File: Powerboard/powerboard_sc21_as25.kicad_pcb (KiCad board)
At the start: 4 copper layers, 86.3 x 55.6 mm, 149 parts, among them IC1 BQ24618RGET-iclr, IC2 CP2102, J1 Thermistor Connection 103AT N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, J10 Conn_01x04_Male, J2 Conn_01x02_Male, J3 Conn_01x02_Male, J4 Conn_01x08_Male, J5 Conn_01x04_Male, J6 Conn_01x02_Male, J7 IsolationSwitch, J8 USB_C_Receptacle_USB2.0, J9 Conn_Coaxial, Q1 RSJ250P10TL, Q10 MCH6351, Q2 RSJ250P10TL, Q3 RSJ250P10TL, Q4 RS1G120MN, Q5 RS1G120MN, Q6 MMDT2222A, Q7 RSJ250P10TL, Q8 RSJ250P10TL, Q9 MCH6351, U1 LTC4412xS6, U11 LTC4411, U2 SN65HVD230, U3 ESP32-PICO-D4, U4 SC4216H, U6 LM2679T-3.3-iclr, U7 LM2679T-3.3-iclr, U8 LTC4412xS6, U9 LTC4412xS6

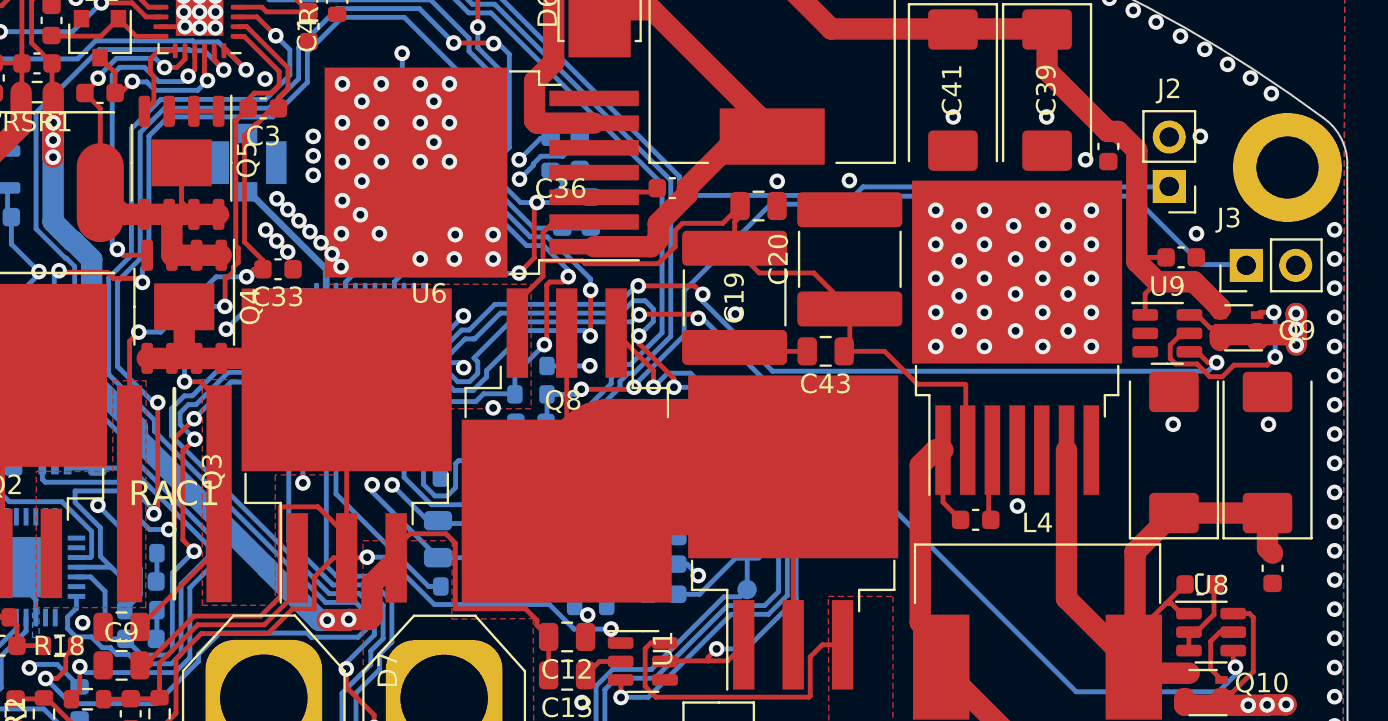
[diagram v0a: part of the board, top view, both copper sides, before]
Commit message: Removed CAN resistors
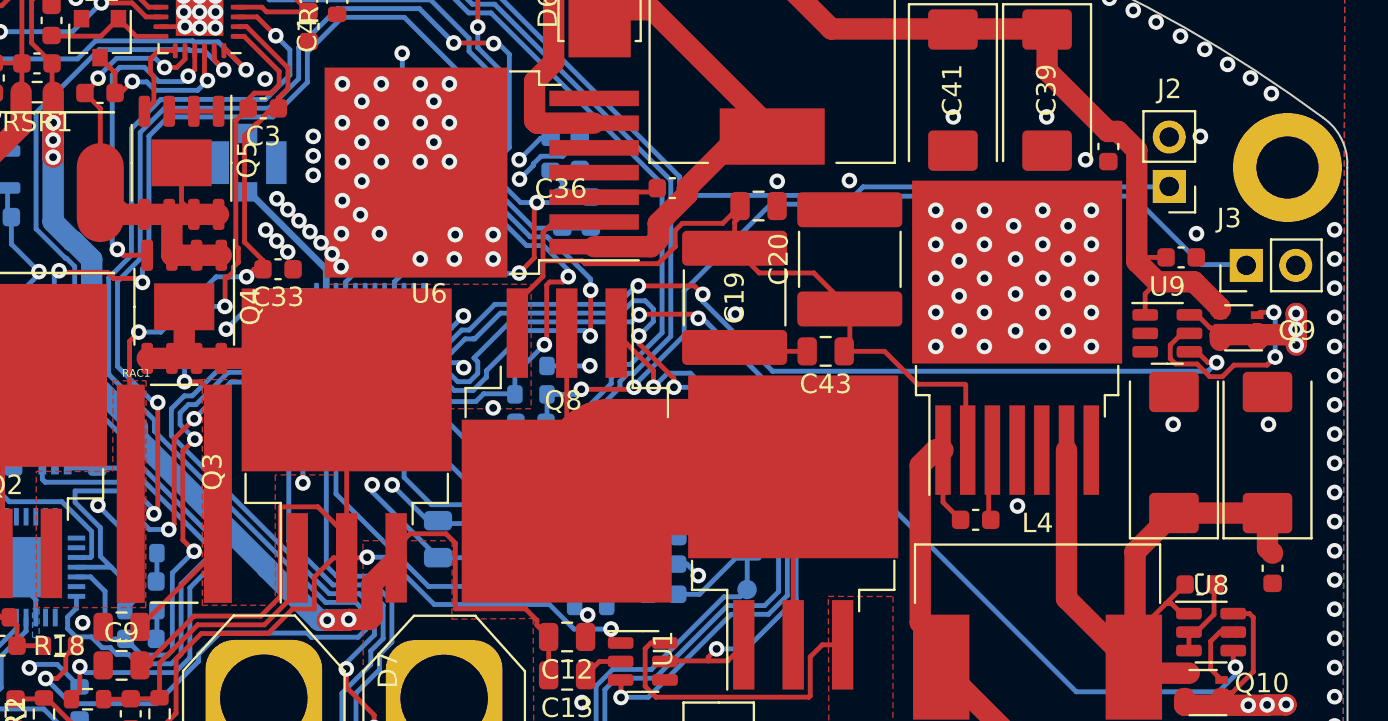
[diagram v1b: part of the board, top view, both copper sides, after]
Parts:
- removed R22, R23: 120, Resistor_SMD:R_0603_1608Metric
- RAC1: footprint iclr:RESC50110X50N -> iclr:RESC50110X70N
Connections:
- U2 pad 1: Net-(R22-Pad2) -> /CAN_TX
- U2 pad 4: Net-(R23-Pad2) -> /CAN_RX
- U3 pad 24: /CAN_RX -> /BATTSTAT2
- U3 pad 25: /BATTSTAT2 -> /CAN_RX
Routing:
- net /BATTSTAT2: track 58.6 -> 53.2 mm
- net /CAN_TX: track 10.9 -> 14.7 mm
- net /CAN_RX: track 3.48 -> 6.47 mm
- net Net-(R23-Pad2): track 2.43 -> 0.00 mm
- net Net-(R22-Pad2): track 2.12 -> 0.00 mm

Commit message: Added connector for PDU EN pin and external LED + routing changes
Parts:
- added J11: Conn_01x03_MountingPin, Connector_Molex:Molex_PicoBlade_53261-0371_1x03-1MP_P1.25mm_Horizontal, B.Cu at (132.4, 65.7)
- moved C18 0.71 mm to (93.2, 57.6)
- moved R11 0.71 mm to (93.2, 54.7)
- moved R8 0.71 mm to (93.2, 56.2)
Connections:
- U3 pad 12: unconnected-(U3-Pad12) -> /3.3STAT1
- U3 pad 13: unconnected-(U3-Pad13) -> /LPC_24V
- U3 pad 14: unconnected-(U3-Pad14) -> /3.3STAT2
- U3 pad 15: unconnected-(U3-Pad15) -> /PG
- U3 pad 16: GND -> /BATTSTAT2
- U3 pad 17: /3.3STAT1 -> /BATTSTAT1
- U3 pad 18: /LPC_24V -> unconnected-(U3-Pad18)
- U3 pad 20: /3.3STAT2 -> GND
- U3 pad 21: /PG -> unconnected-(U3-Pad21)
- U3 pad 24: /BATTSTAT2 -> /EXT_LED
- U3 pad 25: /CAN_RX -> /PDU_EN
- U3 pad 27: /BATTSTAT1 -> /CAN_RX
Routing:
- net /PDU_EN: track 0.00 -> 50.1 mm, vias 0 -> 2
- net /EXT_LED: track 0.00 -> 49.0 mm, vias 0 -> 2
- net GND: track 46.1 -> 58.1 mm, vias 263 -> 264
- net /BATTSTAT1: track 57.3 -> 48.2 mm
- net Net-(Q7-Pad1): track 30.0 -> 33.8 mm
- net /LPC_24V: track 43.0 -> 46.4 mm
- net /Battery Charger/PH: track 26.4 -> 29.4 mm
- net /3.3STAT2: track 53.1 -> 55.7 mm
- net /BATTSTAT2: track 53.2 -> 51.0 mm
- net /BOOT: track 66.7 -> 68.0 mm
- net /PG: track 44.9 -> 43.7 mm
- net /CAN_RX: track 6.47 -> 7.46 mm
- net /EN: track 76.5 -> 77.4 mm
- net /RXD: track 26.1 -> 26.9 mm
- net Net-(J8-PadA5): track 2.66 -> 1.93 mm
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
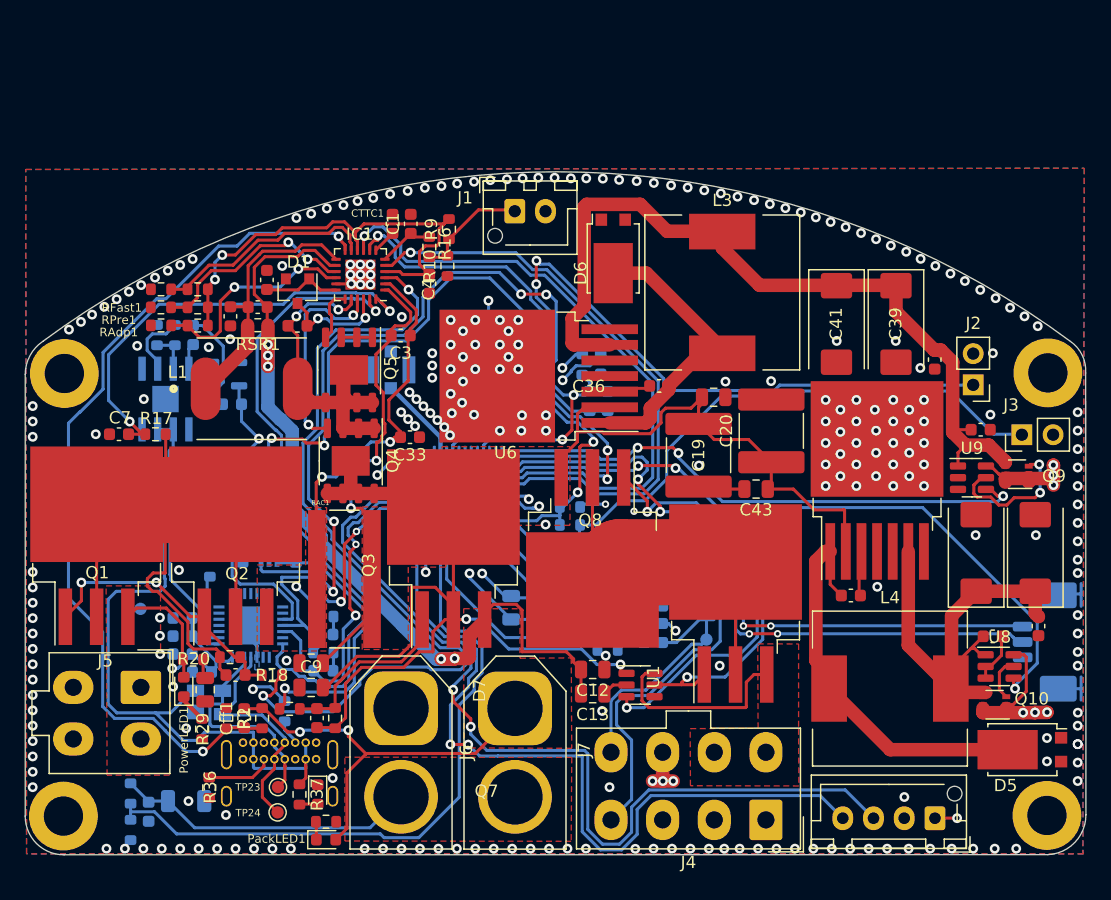
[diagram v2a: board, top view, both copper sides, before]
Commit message: silkscreen tidying
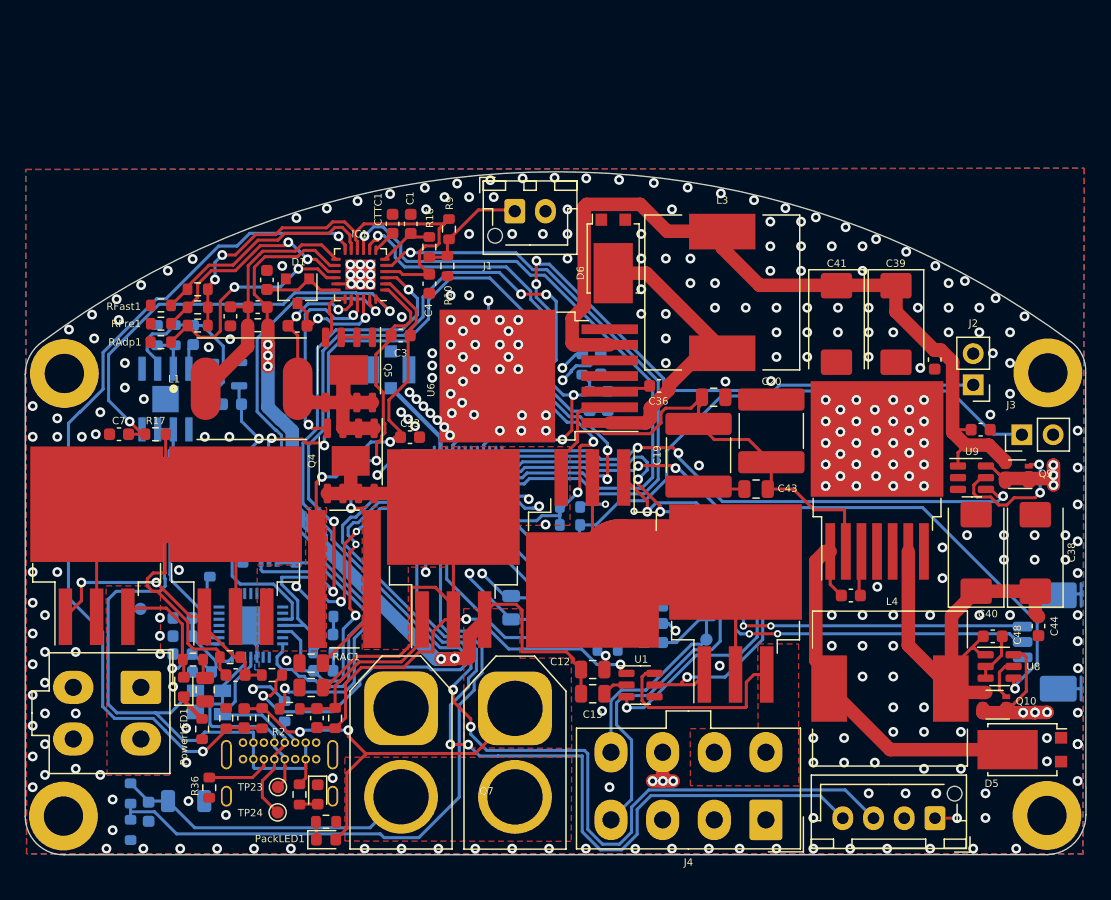
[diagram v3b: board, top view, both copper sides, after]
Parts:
- added G***: LOGO, iclr:MCQUEEN, B.Cu at (114.8, 45.5)
- added G***: LOGO, iclr:iclr_logo, B.Cu at (118.0, 72.6)
- moved RAdp1 1.36 mm to (59.9, 41.3)
- moved RPre1 1.33 mm to (59.9, 39.8)
- moved RFast1 1.31 mm to (59.9, 38.3)
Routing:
- net /Battery Charger/ACSET: track 17.8 -> 18.4 mm
- net Net-(IC1-Pad11): track 18.3 -> 18.8 mm
- net /Battery Charger/ICSET2: track 17.2 -> 17.8 mm
- net GND: vias 264 -> 310
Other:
- board text added: "Electronics & Payload 2022"

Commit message: swapping mosfets the right way around
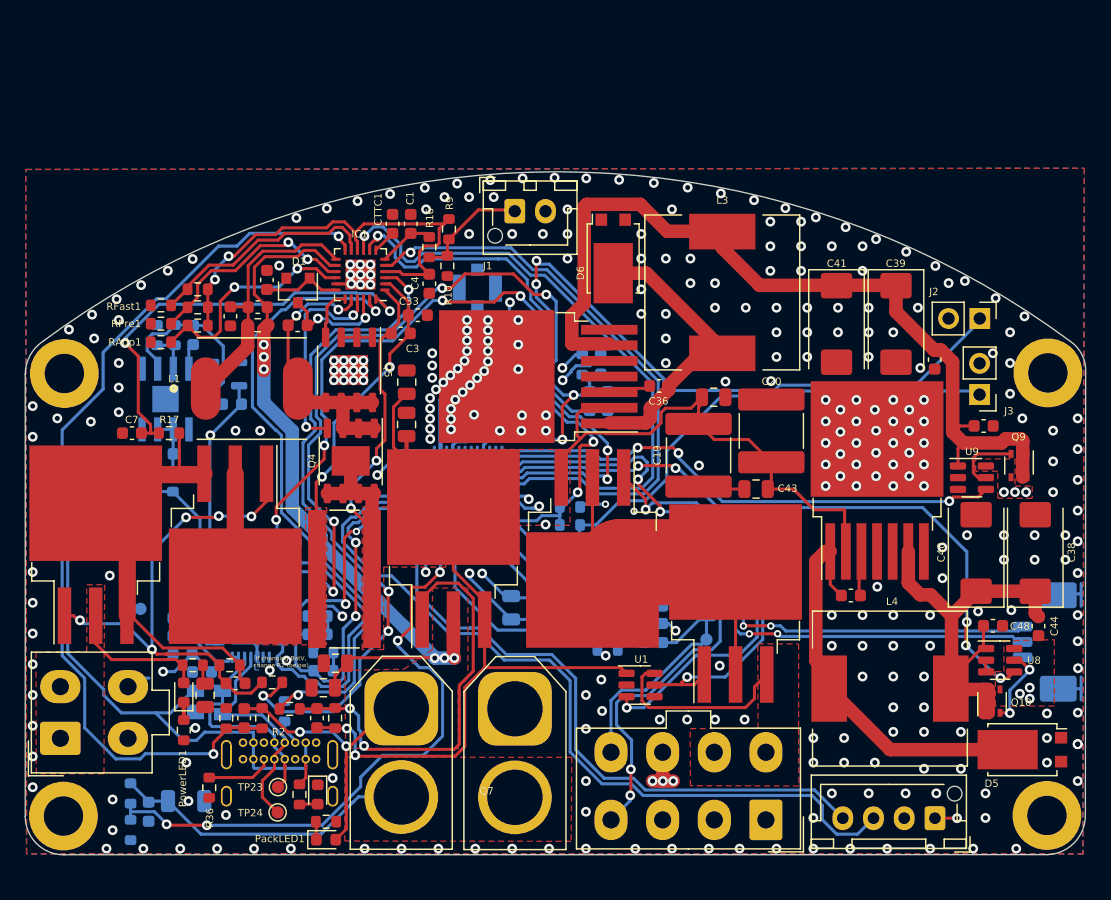
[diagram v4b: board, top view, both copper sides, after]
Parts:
- moved C8 24.1 mm to (79.9, 44.5), turned to -90 degrees
- moved C9 22.8 mm to (79.9, 48.0), turned to -90 degrees
- moved C12 22.0 mm to (73.1, 69.4), turned to 0 degrees
- moved C13 21.1 mm to (74.1, 67.4), turned to 0 degrees
- moved C33 9.94 mm to (80.8, 39.1)
- moved J9 9.68 mm to (85.7, 36.9)
- moved J6 9.27 mm to (88.7, 71.1)
- moved J7 9.25 mm to (79.5, 71.1)
- moved J5 7.75 mm to (51.8, 73.5), turned to 90 degrees
- moved J2 5.42 mm to (126.5, 39.4), turned to -90 degrees
- moved J3 4.74 mm to (126.5, 45.6), turned to 180 degrees
- moved R29 1.49 mm to (61.8, 72.9)
- moved R17 1.11 mm to (60.6, 48.7)
- moved C7 1.06 mm to (57.6, 48.7)
- moved C48 0.86 mm to (127.6, 64.4)
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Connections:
- C11 pad 1: /Battery Charger/Q3-S -> /Battery Charger/Q3-D
- C12 pad 2: /Battery Charger/Q3-S -> /Battery Charger/Q3-D
- C13 pad 2: /Battery Charger/Q3-S -> /Battery Charger/Q3-D
- C14 pad 1: /Battery Charger/Q1-D -> /Battery Charger/Q1-S
- Cff1 pad 2: /Battery Charger/Q3-S -> /Battery Charger/Q3-D
- IC1 pad 14: /Battery Charger/Q3-S -> /Battery Charger/Q3-D
- J7 pad 1: /Battery Charger/Q3-S -> /Battery Charger/Q3-D
- PackLED1 pad 2: /Battery Charger/Q3-S -> /Battery Charger/Q3-D
- Q1 pad 2: /Battery Charger/Q1-D -> Net-(J5-Pad1)
- Q1 pad 3: Net-(J5-Pad1) -> /Battery Charger/Q1-S
- Q10 pad 1: +3V3 -> Net-(C38-Pad1)
- Q10 pad 2: +3V3 -> Net-(C38-Pad1)
- Q10 pad 4: Net-(C38-Pad1) -> +3V3
- Q10 pad 5: +3V3 -> Net-(C38-Pad1)
- Q10 pad 6: +3V3 -> Net-(C38-Pad1)
- Q2 pad 2: /Battery Charger/Q1-D -> Net-(C3-Pad1)
- Q2 pad 3: Net-(C3-Pad1) -> /Battery Charger/Q1-S
- Q3 pad 2: +24V -> /Battery Charger/Q3-D
- Q3 pad 3: /Battery Charger/Q3-S -> +24V
- Q5 pad 9: /Battery Charger/PH -> GND
- Q9 pad 1: +3V3 -> Net-(C39-Pad1)
- Q9 pad 2: +3V3 -> Net-(C39-Pad1)
- Q9 pad 4: Net-(C39-Pad1) -> +3V3
- Q9 pad 5: +3V3 -> Net-(C39-Pad1)
- Q9 pad 6: +3V3 -> Net-(C39-Pad1)
- R14 pad 1: /Battery Charger/Q1-D -> /Battery Charger/Q1-S
- R17 pad 2: /Battery Charger/Q1-D -> /Battery Charger/Q1-S
- R2 pad 2: /Battery Charger/Q3-S -> /Battery Charger/Q3-D
- RSR1 pad 1: /Battery Charger/Q3-S -> /Battery Charger/Q3-D
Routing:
- net /Battery Charger/Q3-S: track 103.7 -> 0.00 mm, vias 7 -> 0
- net /Battery Charger/Q3-D: track 0.00 -> 88.1 mm, vias 0 -> 8
- net /Battery Charger/Q1-D: track 54.7 -> 0.00 mm
- net /Battery Charger/Q1-S: track 0.00 -> 35.9 mm
- net Net-(C15-Pad2): track 15.0 -> 35.0 mm, vias 0 -> 2
- net +3V3: track 101.6 -> 82.5 mm
- net /Battery Charger/Q1-G: track 22.2 -> 40.9 mm, vias 2 -> 5
- net GND: track 58.1 -> 44.0 mm, vias 310 -> 311
- net /SCL: track 65.9 -> 52.6 mm, vias 2 -> 0
- net Net-(IC1-Pad3): track 68.2 -> 56.3 mm, vias 2 -> 4
- net /SDA: track 75.2 -> 66.7 mm, vias 2 -> 0
- net /LNA_IN: track 6.89 -> 13.0 mm
- net /Battery Charger/PH: track 29.4 -> 23.4 mm
- net Net-(C3-Pad1): track 31.7 -> 37.5 mm
- net Net-(Q9-Pad3): track 11.4 -> 5.61 mm, vias 2 -> 0
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- added copper zone on F.Cu, net +3V3
- added copper zone on F.Cu, net /Battery Charger/Q3-D
- removed copper zone on F.Cu, net /Battery Charger/Q3-S
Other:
- outline, holes or cut-outs redrawn
- board text added: "If changing BatV, change R2 (below)"
